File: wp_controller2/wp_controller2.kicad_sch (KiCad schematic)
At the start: 33 parts, among them J12 P sensor, J13 Q meter, J14 220V, J15 q_meter, J16 ACS712, J17 DV_sense, J18 p_sensor, J19 5V, J20 pump ON/OFF, J21 LCD, J22 L298x2, J23 DV1, J24 cmd, J25 CMD, J26 DV act, J27 DV act, J28 DV_sense, J29 Pump ON/OFF, J30 Power, J31 Pump power, J33 DV0, J34 Power, J35 DV_sense, J36 cmd, J37 DV1, J39 DV0, J40 rot enc, J43 12V, J44 12V, J45 12V, J46 220V, J47 220V

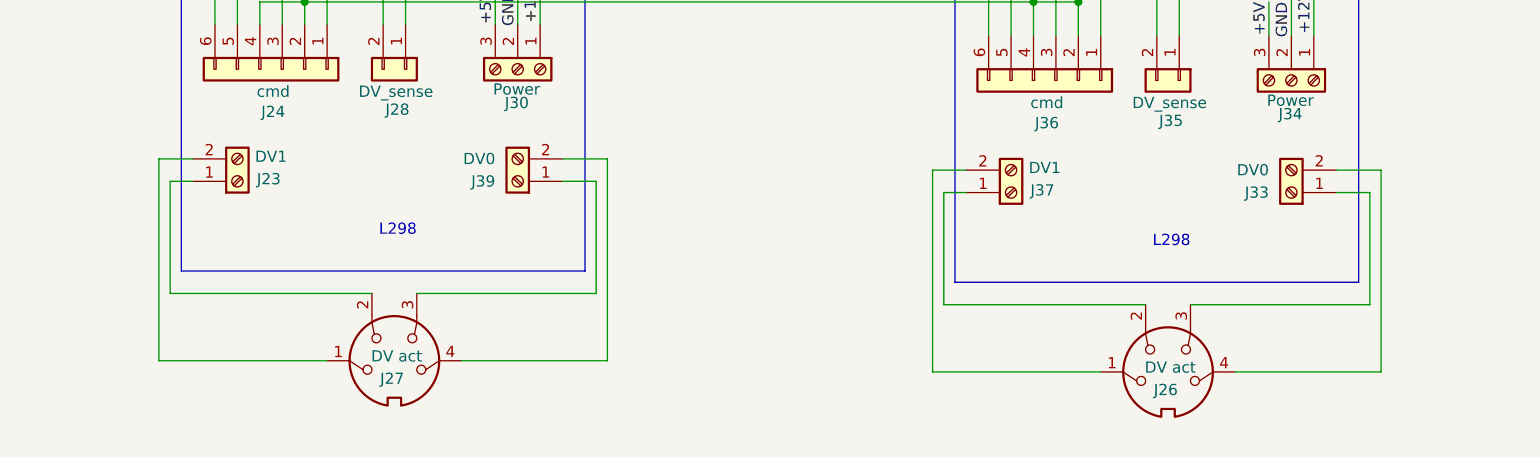
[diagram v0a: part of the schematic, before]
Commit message: 8 pin connector for DVs
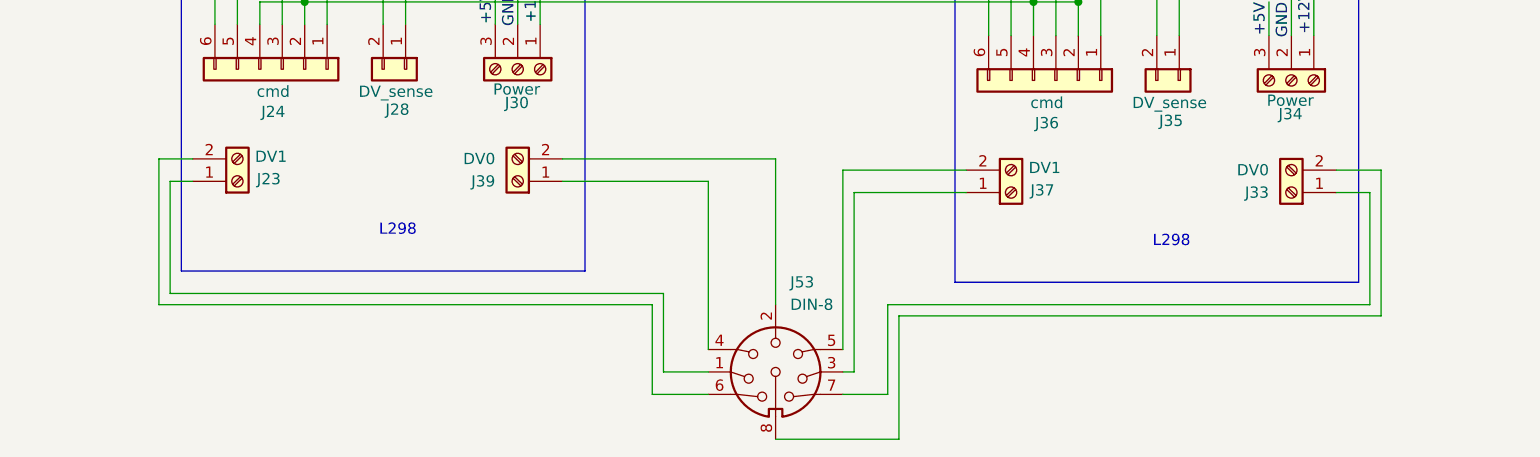
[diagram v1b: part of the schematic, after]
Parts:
- removed J26, J27: DV act, symbol Connector:DIN-4
- added J53: DIN-8, symbol Connector:DIN-8
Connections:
- net at J37.2 (Pin_2): now also J53.5
- net at J37.1 (Pin_1): now also J53.3
- net at J33.1 (Pin_1): now also J53.7
- net at J33.2 (Pin_2): now also J53.8
- net at J23.2 (Pin_2): now also J53.6
- net at J23.1 (Pin_1): now also J53.1
- net at J39.1 (Pin_1): now also J53.4
- net at J39.2 (Pin_2): now also J53.2
